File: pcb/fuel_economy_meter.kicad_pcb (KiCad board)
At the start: 2 copper layers, 40.4 x 54.4 mm, 14 parts, among them J1 Conn_01x02_Female, J2 Conn_01x02_Female, U1 MAX9924UAUB+T, U2 ESP32-DEVKIT-V1

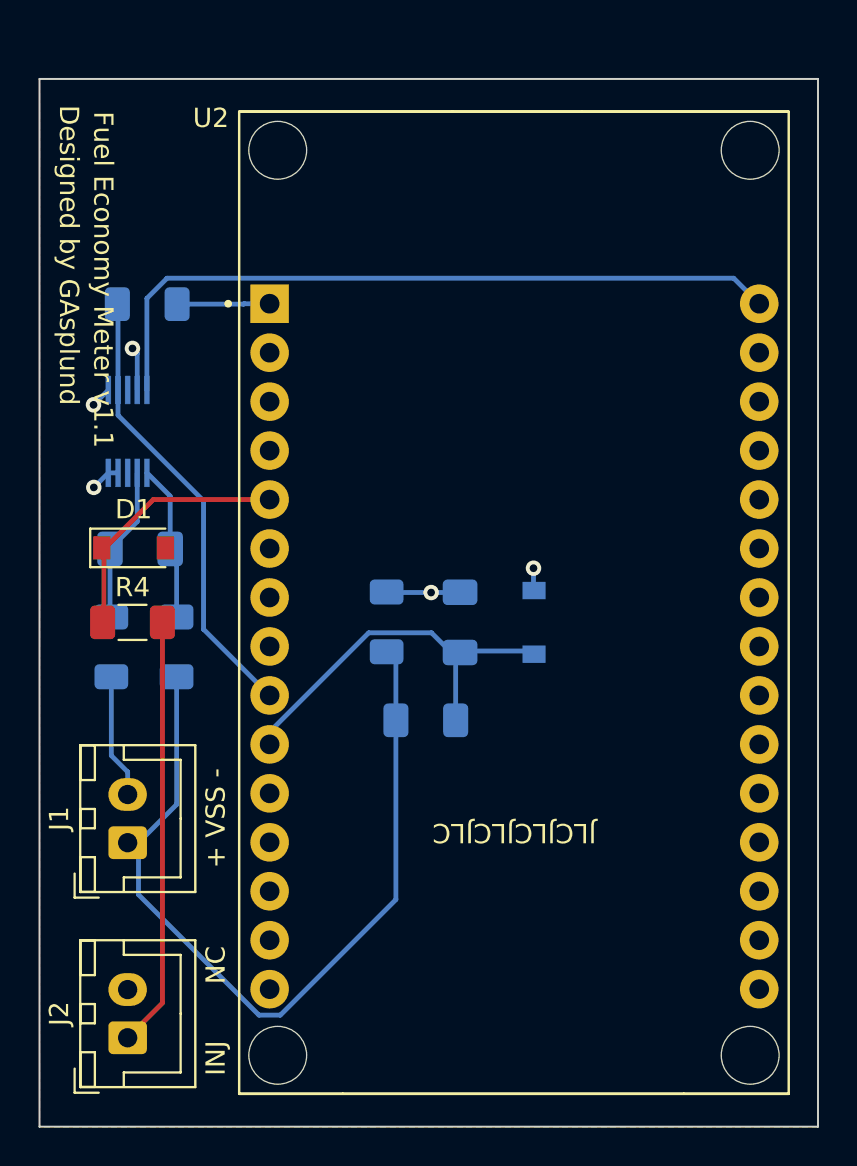
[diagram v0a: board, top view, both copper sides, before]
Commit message: Remove VR sensor circuit
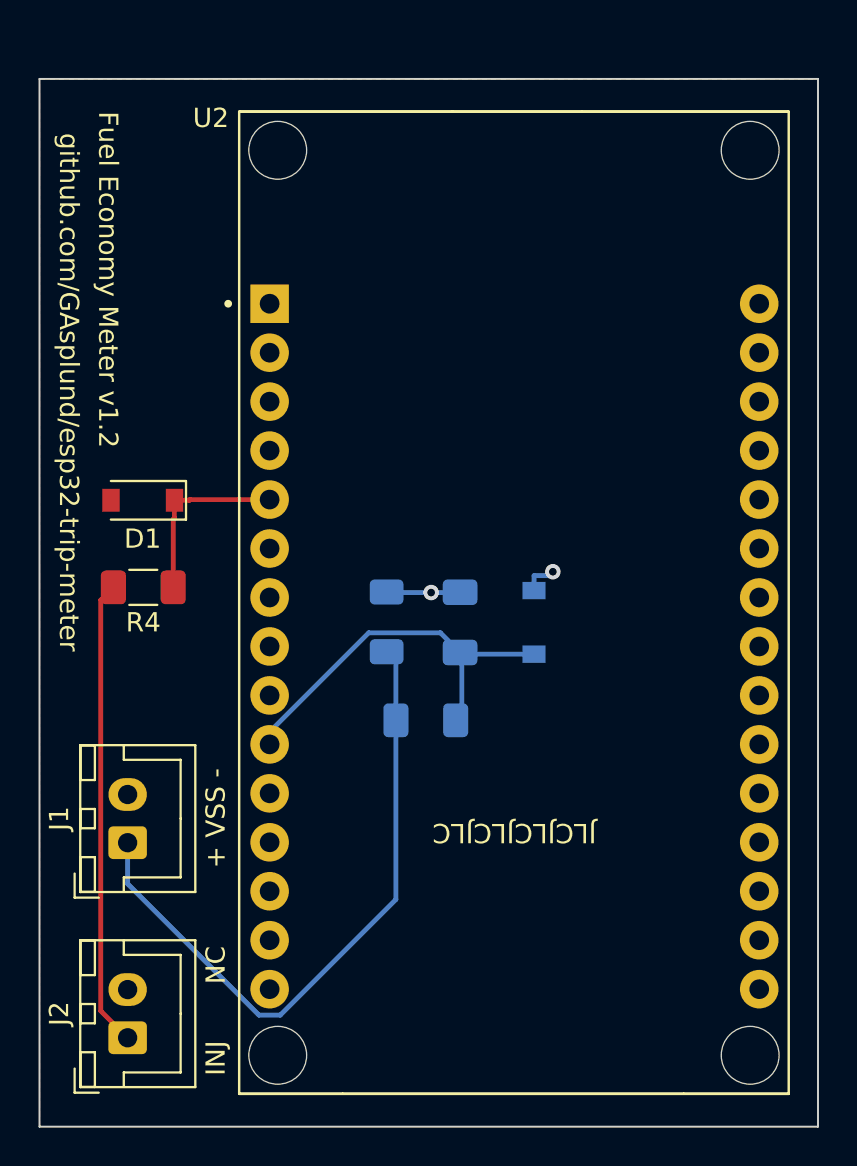
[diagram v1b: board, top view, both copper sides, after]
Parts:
- removed C1: 1nF, Capacitor_SMD:C_1206_3216Metric_Pad1.33x1.80mm_HandSolder
- removed R1, R2, R3: 10K, Resistor_SMD:R_1206_3216Metric_Pad1.30x1.75mm_HandSolder
- removed U1: MAX9924UAUB+T, Package_SO_Custom:SOP50P490X110-10N
- moved D1 2.51 mm to (127.3, 78.2), turned to 180 degrees
- moved R4 1.90 mm to (127.3, 82.8), turned to 180 degrees
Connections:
- net Net-(D1-Pad1) renamed /INJ_SIG
- J2 pad 2: unconnected-(J2-Pad2) -> GND
- U2 pad 9: VSS_OUT -> unconnected-(U2-Pad9)
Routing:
- net 5V: track 37.5 -> 0.00 mm
- net VSS_OUT: track 23.6 -> 0.00 mm
- net VSS+: track 44.2 -> 34.4 mm
- net Net-(C1-Pad1): track 8.11 -> 0.00 mm
- net Net-(C1-Pad2): track 8.09 -> 0.00 mm
- net VSS-: track 6.46 -> 0.00 mm
- net 3v3: track 4.81 -> 0.00 mm
- net GND: track 10.1 -> 5.66 mm, vias 5 -> 2
- net /INJ_SIG: track 13.5 -> 9.50 mm
- net INJ_GND: track 22.3 -> 24.2 mm
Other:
- board text added: "Fuel Economy Meter v1.2"
- board text added: "github.com/GAsplund/esp32-trip-meter"
- board text removed: "Designed by GAsplund"
- board text removed: "Fuel Economy Meter v1.1"

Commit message: Don't use strapping pin for injector signal
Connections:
- U2 pad 5: /INJ_SIG -> unconnected-(U2-Pad5)
- U2 pad 9: unconnected-(U2-Pad9) -> /INJ_SIG
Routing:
- net /INJ_SIG: track 9.50 -> 12.2 mm
- net GND: track 5.66 -> 4.61 mm, vias 2 -> 3
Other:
- board text added: "GND"
- board text removed: "NC"
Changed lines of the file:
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@@
   (net 29 "5V")
   (net 30 "unconnected-(U2-Pad15)")
-  (net 31 "unconnected-(U2-Pad9)")
+  (net 31 "unconnected-(U2-Pad5)")
   (net 32 "/INJ_SIG")
   (footprint "Connector_JST:JST_XH_B2B-XH-A_1x02_P2.50mm_Vertical" (layer "F.Cu")
@@
       (net 7 "unconnected-(U2-Pad4)") (pinfunction "D2") (pintype "bidirectional"))
     (pad "5" thru_hole circle (at -12.7 -5.355) (size 2 2) (drill 1.02) (layers *.Cu *.Mask)
-      (net 32 "/INJ_SIG") (pinfunction "D4") (pintype "bidirectional"))
+      (net 31 "unconnected-(U2-Pad5)") (pinfunction "D4") (pintype "bidirectional"))
     (pad "6" thru_hole circle (at -12.7 -2.815) (size 2 2) (drill 1.02) (layers *.Cu *.Mask)
       (net 9 "unconnected-(U2-Pad6)") (pinfunction "RX2") (pintype "input"))
@@
       (net 11 "unconnected-(U2-Pad8)") (pinfunction "D5") (pintype "bidirectional"))
     (pad "9" thru_hole circle (at -12.7 4.805) (size 2 2) (drill 1.02) (layers *.Cu *.Mask)
-      (net 31 "unconnected-(U2-Pad9)") (pinfunction "D18") (pintype "bidirectional"))
+      (net 32 "/INJ_SIG") (pinfunction "D18") (pintype "bidirectional"))
     (pad "10" thru_hole circle (at -12.7 7.345) (size 2 2) (drill 1.02) (layers *.Cu *.Mask)
       (net 8 "VSS_A") (pinfunction "D19") (pintype "bidirectional"))
@@
     (effects (font (size 1 1) (thickness 0.18)))
   )
-  (gr_text "NC" (at 131.064 102.362 90) (layer "F.SilkS")
+  (gr_text "GND" (at 131.064 103.378 90) (layer "F.SilkS")
     (effects (font (size 1 1) (thickness 0.15)))
   )
@@
     (effects (font (size 1 1) (thickness 0.15)))
   )
+  (via (at 143.738 81.7333) (size 0.8) (drill 0.4) (layers "F.Cu" "B.Cu") (net 2))
+  (via (at 138.4485 83.0339) (size 0.8) (drill 0.4) (layers "F.Cu" "B.Cu") (net 2))
   (via (at 148.5515 81.9545) (size 0.8) (drill 0.4) (layers "F.Cu" "B.Cu") (net 2))
-  (via (at 142.2367 83.0344) (size 0.8) (drill 0.4) (layers "F.Cu" "B.Cu") (net 2))
-  (segment (start 139.9564 83.0344) (end 139.928 83.006) (width 0.25) (layer "B.Cu") (net 2))
-  (segment (start 143.738 83.0195) (end 143.7231 83.0344) (width 0.25) (layer "B.Cu") (net 2))
+  (segment (start 138.4485 83.0339) (end 139.9001 83.0339) (width 0.25) (layer "B.Cu") (net 2))
+  (segment (start 143.738 83.0195) (end 143.738 81.7333) (width 0.25) (layer "B.Cu") (net 2))
+  (segment (start 148.3491 82.1569) (end 147.574 82.1569) (width 0.25) (layer "B.Cu") (net 2))
   (segment (start 147.574 82.932) (end 147.574 82.1569) (width 0.25) (layer "B.Cu") (net 2))
-  (segment (start 148.3491 82.1569) (end 147.574 82.1569) (width 0.25) (layer "B.Cu") (net 2))
-  (segment (start 142.2367 83.0344) (end 139.9564 83.0344) (width 0.25) (layer "B.Cu") (net 2))
-  (segment (start 143.7231 83.0344) (end 142.2367 83.0344) (width 0.25) (layer "B.Cu") (net 2))
+  (segment (start 139.9001 83.0339) (end 139.928 83.006) (width 0.25) (layer "B.Cu") (net 2))
   (segment (start 148.5515 81.9545) (end 148.3491 82.1569) (width 0.25) (layer "B.Cu") (net 2))
+  (segment (start 140.41 86.588) (end 140.41 89.662) (width 0.25) (layer "B.Cu") (net 3))
+  (segment (start 133.3056 104.9575) (end 134.4126 104.9575) (width 0.25) (layer "B.Cu") (net 3))
+  (segment (start 126.492 98.1439) (end 133.3056 104.9575) (width 0.25) (layer "B.Cu") (net 3))
   (segment (start 126.492 96.012) (end 126.492 98.1439) (width 0.25) (layer "B.Cu") (net 3))
   (segment (start 140.41 98.9601) (end 140.41 89.662) (width 0.25) (layer "B.Cu") (net 3))
   (segment (start 134.4126 104.9575) (end 140.41 98.9601) (width 0.25) (layer "B.Cu") (net 3))
-  (segment (start 133.3056 104.9575) (end 134.4126 104.9575) (width 0.25) (layer "B.Cu") (net 3))
-  (segment (start 126.492 98.1439) (end 133.3056 104.9575) (width 0.25) (layer "B.Cu") (net 3))
-  (segment (start 140.41 86.588) (end 140.41 89.662) (width 0.25) (layer "B.Cu") (net 3))
   (segment (start 139.928 86.106) (end 140.41 86.588) (width 0.25) (layer "B.Cu") (net 3))
+  (segment (start 125.754 82.766) (end 125.0978 83.4222) (width 0.25) (layer "F.Cu") (net 5))
   (segment (start 125.0978 104.7378) (end 126.492 106.132) (width 0.25) (layer "F.Cu") (net 5))
-  (segment (start 125.754 82.766) (end 125.0978 83.4222) (width 0.25) (layer "F.Cu") (net 5))
   (segment (start 125.0978 83.4222) (end 125.0978 104.7378) (width 0.25) (layer "F.Cu") (net 5))
+  (segment (start 142.7142 85.1207) (end 143.738 86.1445) (width 0.25) (layer "B.Cu") (net 8))
+  (segment (start 147.574 86.232) (end 143.8255 86.232) (width 0.25) (layer "B.Cu") (net 8))
   (segment (start 133.858 90.911) (end 133.858 90.263) (width 0.25) (layer "B.Cu") (net 8))
-  (segment (start 147.574 86.232) (end 143.8255 86.232) (width 0.25) (layer "B.Cu") (net 8))
+  (segment (start 143.8255 89.3465) (end 143.51 89.662) (width 0.25) (layer "B.Cu") (net 8))
   (segment (start 143.8255 86.232) (end 143.738 86.1445) (width 0.25) (layer "B.Cu") (net 8))
   (segment (start 133.858 90.263) (end 139.0003 85.1207) (width 0.25) (layer "B.Cu") (net 8))
+  (segment (start 143.8255 86.232) (end 143.8255 89.3465) (width 0.25) (layer "B.Cu") (net 8))
   (segment (start 139.0003 85.1207) (end 142.7142 85.1207) (width 0.25) (layer "B.Cu") (net 8))
-  (segment (start 142.7142 85.1207) (end 143.738 86.1445) (width 0.25) (layer "B.Cu") (net 8))
-  (segment (start 143.8255 86.232) (end 143.8255 89.3465) (width 0.25) (layer "B.Cu") (net 8))
-  (segment (start 143.8255 89.3465) (end 143.51 89.662) (width 0.25) (layer "B.Cu") (net 8))
-  (segment (start 129.7321 78.211) (end 129.6951 78.248) (width 0.25) (layer "F.Cu") (net 32))
+  (segment (start 128.854 83.367) (end 128.854 82.766) (width 0.25) (layer "F.Cu") (net 32))
+  (segment (start 133.858 88.371) (end 128.854 83.367) (width 0.25) (layer "F.Cu") (net 32))
   (segment (start 128.854 82.766) (end 128.854 79.2391) (width 0.25) (layer "F.Cu") (net 32))
-  (segment (start 133.858 78.211) (end 129.7321 78.211) (width 0.25) (layer "F.Cu") (net 32))
+  (segment (start 128.92 78.248) (end 128.92 79.1731) (width 0.25) (layer "F.Cu") (net 32))
   (segment (start 128.854 79.2391) (end 128.92 79.1731) (width 0.25) (layer "F.Cu") (net 32))
-  (segment (start 128.92 78.248) (end 129.6951 78.248) (width 0.25) (layer "F.Cu") (net 32))
-  (segment (start 128.92 78.248) (end 128.92 79.1731) (width 0.25) (layer "F.Cu") (net 32))
   (zone (net 2) (net_name "GND") (layer "F.Cu") (hatch edge 0.508)
     (connect_pads (clearance 0.254))

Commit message: Consolidate component designators
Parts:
- renumbered C2 to C1, D2 to D1, D1 to D2, R5 to R1, R6 to R2, R4 to R3, U2 to U1
